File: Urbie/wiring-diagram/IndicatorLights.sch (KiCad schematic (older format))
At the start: 9 parts

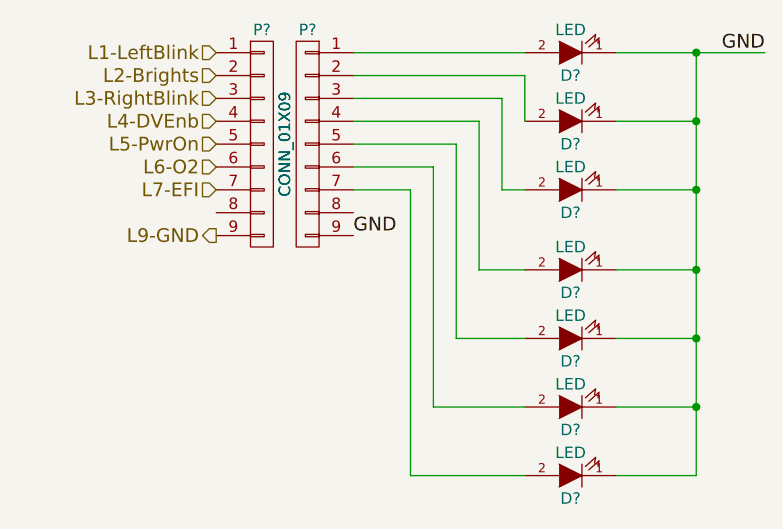
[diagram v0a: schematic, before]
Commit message: cleaning up schematics
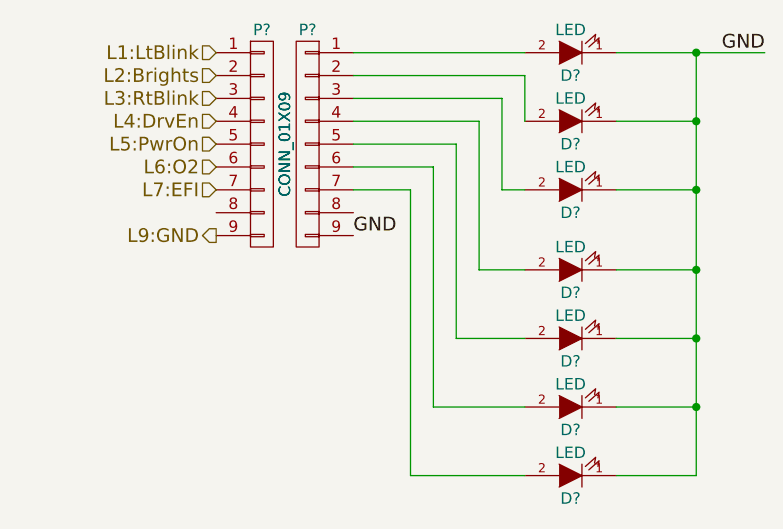
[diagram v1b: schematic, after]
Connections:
- net L1-LeftBlink renamed L1:LtBlink
- net L2-Brights renamed L2:Brights
- net L3-RightBlink renamed L3:RtBlink
- net L4-DVEnb renamed L4:DrvEn
- net L5-PwrOn renamed L5:PwrOn
- net L6-O2 renamed L6:O2
- net L7-EFI renamed L7:EFI
- net L9-GND renamed L9:GND
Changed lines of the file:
@@
 $EndDescr
 Text HLabel 3450 3500 0    60   Input ~ 0
-L1-LeftBlink
+L1:LtBlink
 Text HLabel 3450 3700 0    60   Input ~ 0
-L3-RightBlink
+L3:RtBlink
 Text HLabel 3450 3600 0    60   Input ~ 0
-L2-Brights
+L2:Brights
 Text HLabel 3450 3800 0    60   Input ~ 0
-L4-DVEnb
+L4:DrvEn
 Text HLabel 3450 3900 0    60   Input ~ 0
-L5-PwrOn
+L5:PwrOn
 Text HLabel 3450 4000 0    60   Input ~ 0
-L6-O2
+L6:O2
 Text HLabel 3450 4100 0    60   Input ~ 0
-L7-EFI
+L7:EFI
 $Comp
 L LED D?
@@
 Connection ~ 5550 5050
 Text HLabel 3450 4300 0    60   Output ~ 0
-L9-GND
+L9:GND
 Connection ~ 5550 3500
 Wire Wire Line

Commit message: I don't know what changed
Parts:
- D? (x7): symbol LED -> LED-RESCUE-Version1
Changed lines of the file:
@@
 EESchema Schematic File Version 2
+LIBS:Version1-rescue
 LIBS:power
 LIBS:device
@@
 L7:EFI
 $Comp
-L LED D?
+L LED-RESCUE-Version1 D?
 U 1 1 57EFD4D4
 P 5000 3500
@@
 $EndComp
 $Comp
-L LED D?
+L LED-RESCUE-Version1 D?
 U 1 1 57EFD562
 P 5000 4450
@@
 $EndComp
 $Comp
-L LED D?
+L LED-RESCUE-Version1 D?
 U 1 1 57EFD57D
 P 5000 4750
@@
 $EndComp
 $Comp
-L LED D?
+L LED-RESCUE-Version1 D?
 U 1 1 57EFD59B
 P 5000 5050
@@
 $EndComp
 $Comp
-L LED D?
+L LED-RESCUE-Version1 D?
 U 1 1 57EFD5BC
 P 5000 5350
@@
 $EndComp
 $Comp
-L LED D?
+L LED-RESCUE-Version1 D?
 U 1 1 57EFD6C1
 P 5000 3800
@@
 	4600 3800 4050 3800
 $Comp
-L LED D?
+L LED-RESCUE-Version1 D?
 U 1 1 57FA2916
 P 5000 4100
